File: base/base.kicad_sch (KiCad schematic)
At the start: 6 parts, among them J1 DF40GB(1.5)-30DS-0.4V(51), J2 DIP-48_Socket

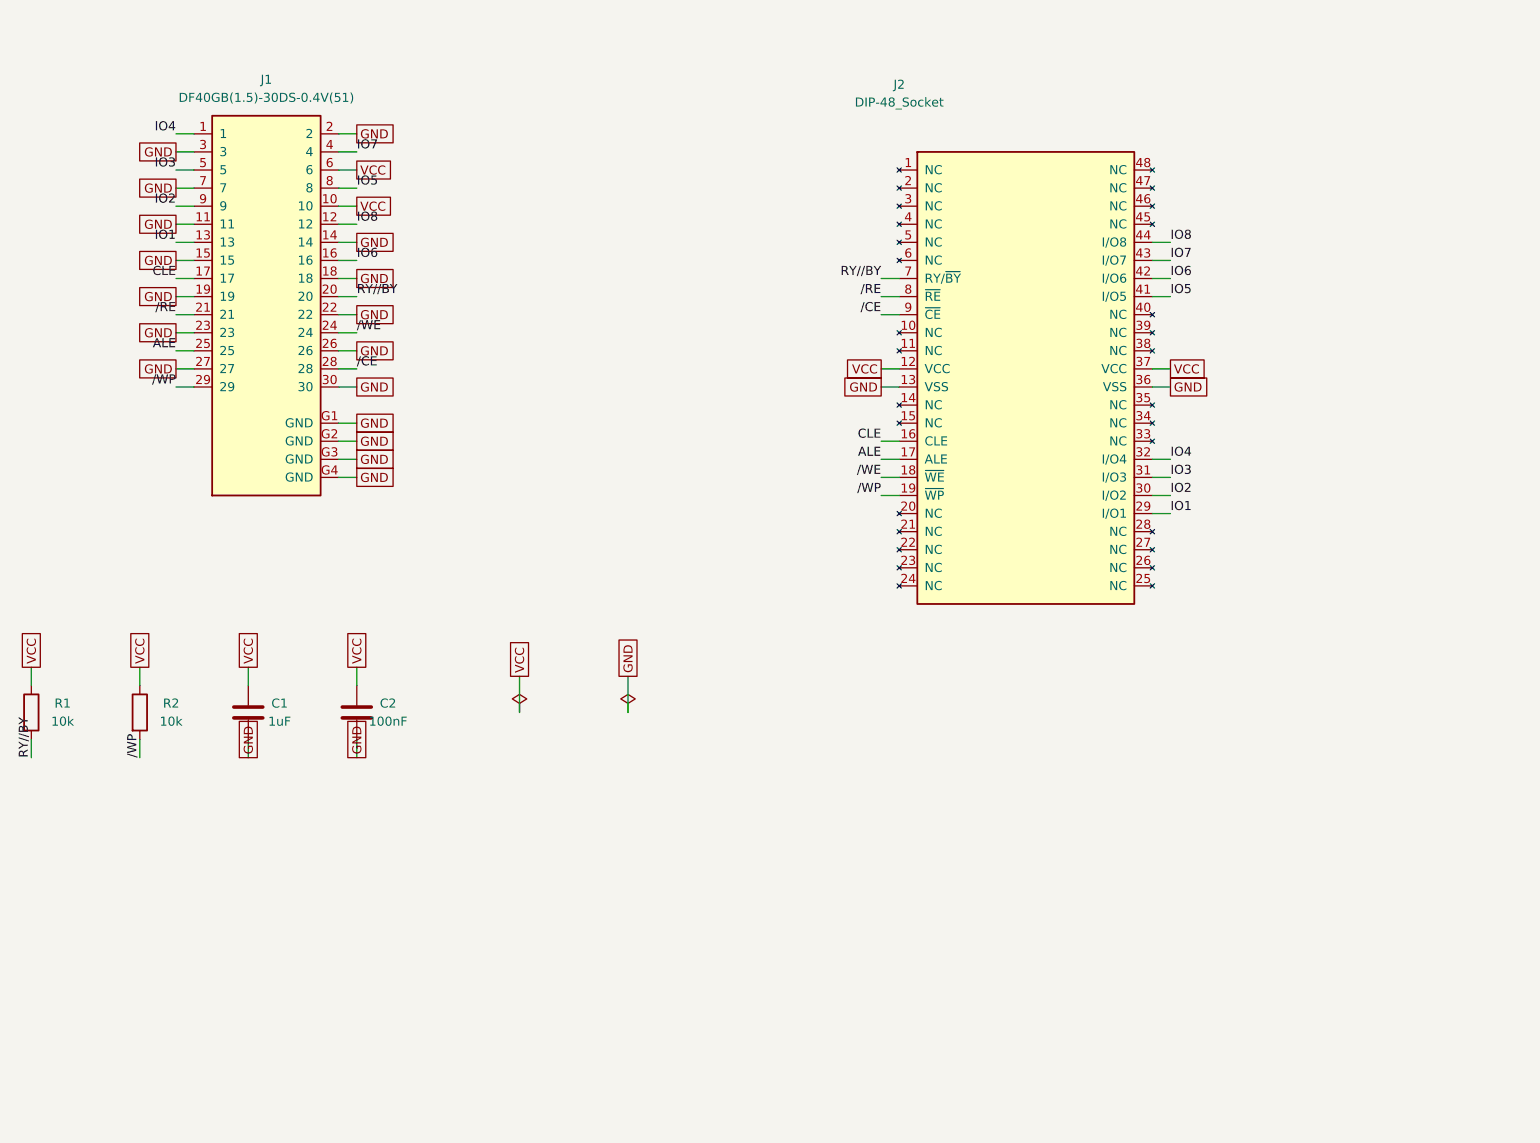
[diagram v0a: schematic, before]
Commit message: Regenerate the panel against Alex's second silk pass
Carrier silk warnings 20 -> 6: the four pin-number texts are gone and U1's
B.SilkS no longer runs off the board edge. What is left is REV A and
VFBGA67, still 0.85 mm / 0.106 mm against JLC's 1.0 / 0.15 legend minimum,
and both crossing J1's silk rectangle.

Panel: 56.80 x 49.60 mm, 16 up, 412 mouse bites, no hard violations.

Also fixed two cosmetic bugs in panelize.sh's own summary -- the board-count
match was missing the library nickname prefix so it always printed 0, and
the outline-extent regex required (layer "Edge.Cuts") at a fixed offset from
(start ...), which it is not, so the size line never printed. Neither
affected the panel itself.
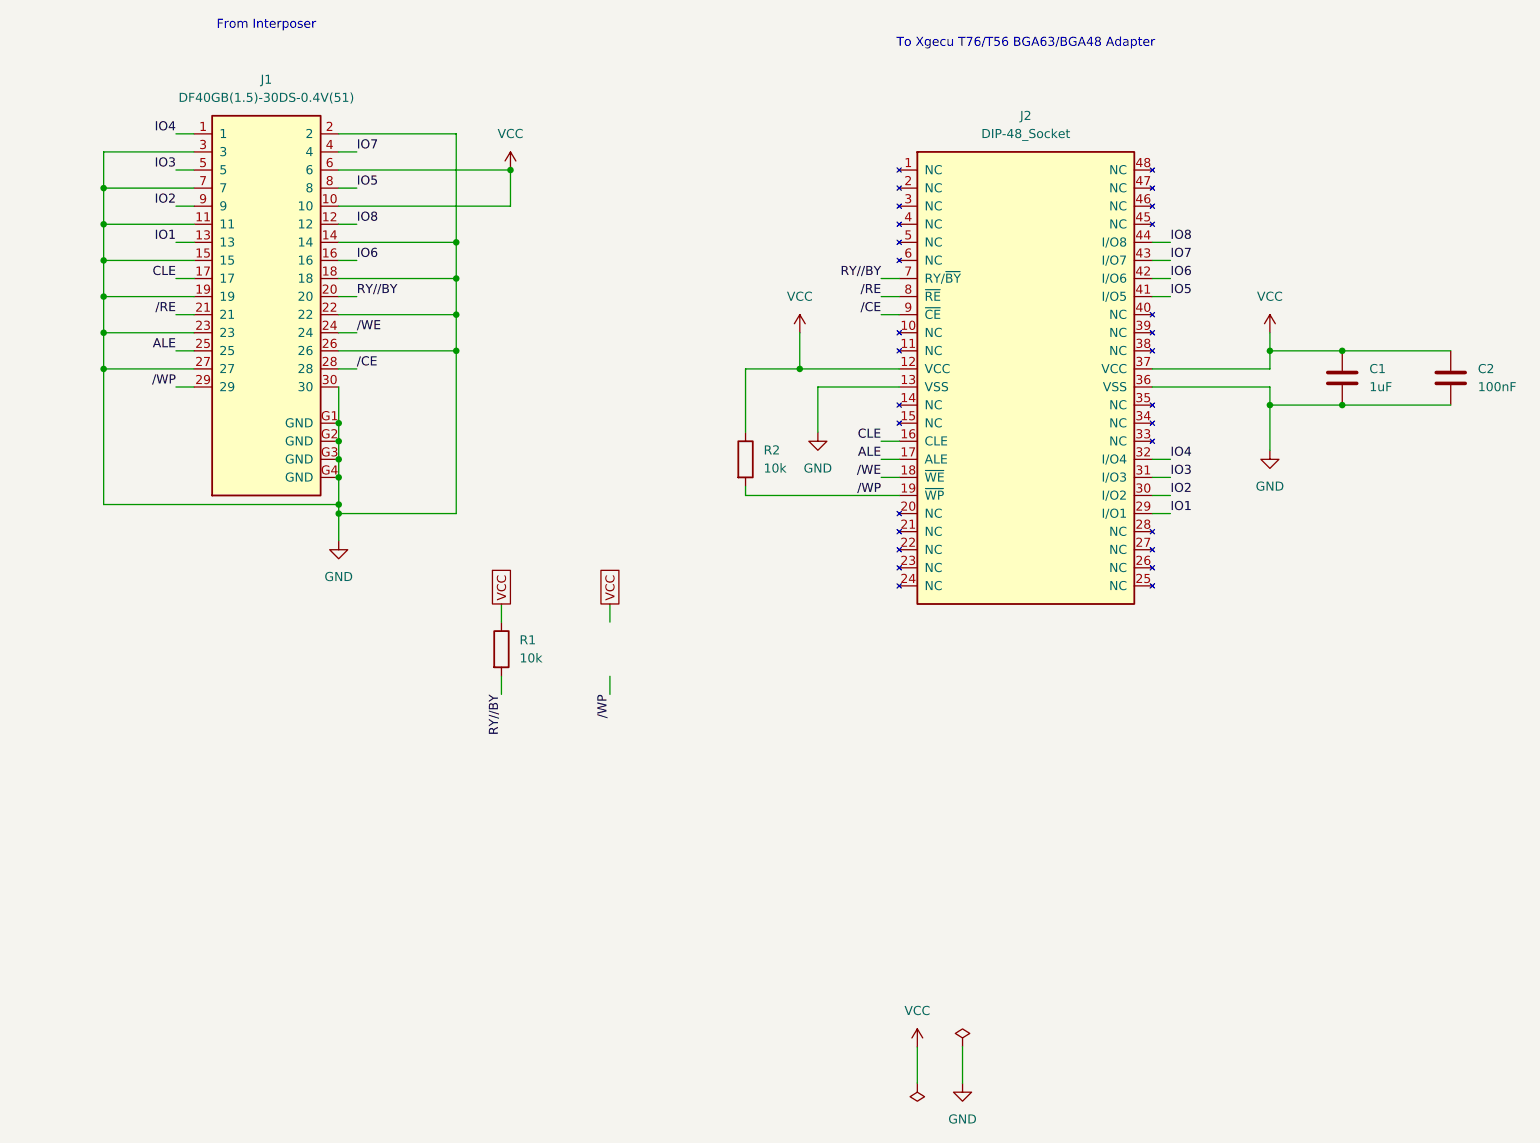
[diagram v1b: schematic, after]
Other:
- note added: "From Interposer"
- note added: "To Xgecu T76/T56 BGA63/BGA48 Adapter"
- moved on the sheet: C1, C2, R1, R2

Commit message: Finish base routing: 16 of 17 connections
tools/route_base.py is additive and re-runnable. It removes only its own
output -- vias and inner-layer tracks -- so Alex's F.Cu/B.Cu hand routing
survives a rerun, and it plans the whole board before committing anything so
a bad net ordering can be thrown away rather than hand-unpicked.

Routed: IO1-IO4, /RE, /ALE, /WP, /WE, /CE, VCC J1.10 and J2.12<->J2.37, and
R1's pull-up tail. Six of these sit on the wrong side of J1 -- IO1-IO4 are on
the odd row but land on the right-hand DIP column, /WE and /CE the reverse --
so they drop to In1/In2 and cross under the connector.

The zone was the reason every J1 GND pad read unconnected: it was on KiCad's
stock 0.5 mm clearance / 0.25 min width / 0.5 thermal gap, and a pour on those
settings cannot approach a 0.4 mm-pitch connector from any direction. Now on
the carrier's 0.2 / 0.15 / 0.3 with solid pad connection. 0.15 is load-bearing:
at 0.25 the pour needs 0.65 mm to reach a GND pad between two escape stubs and
has exactly 0.65, and all 13 go unconnected again.

Bugs found and fixed in my own checker along the way, each caught by DRC
rather than by reading the code:
  - pads were obstacles on every layer, so J1's B.Cu pads walled off both
    inner layers under the connector -- exactly the space the crossing nets
    need
  - track width was assumed 0.15, but Power-class runs are 0.4, under-
    reporting clearance to the VCC tracks by 0.125 mm
  - hole-to-hole was skipped for same-net pads and same-net vias, which
    stacked stitching vias on escape vias (18 holes_co_located)
  - the board edge was taken as a bounding box, but base's outline carries
    (radius 3), so stitching vias landed in corners that do not exist
  - strip() dropped its references to removed items, and pcbnew then freed
    them under the board; GetArea() started returning raw SwigPyObjects

DRC: no clearance, hole or edge violations, 0 unrouted signal nets.

Still open, both needing a decision rather than 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
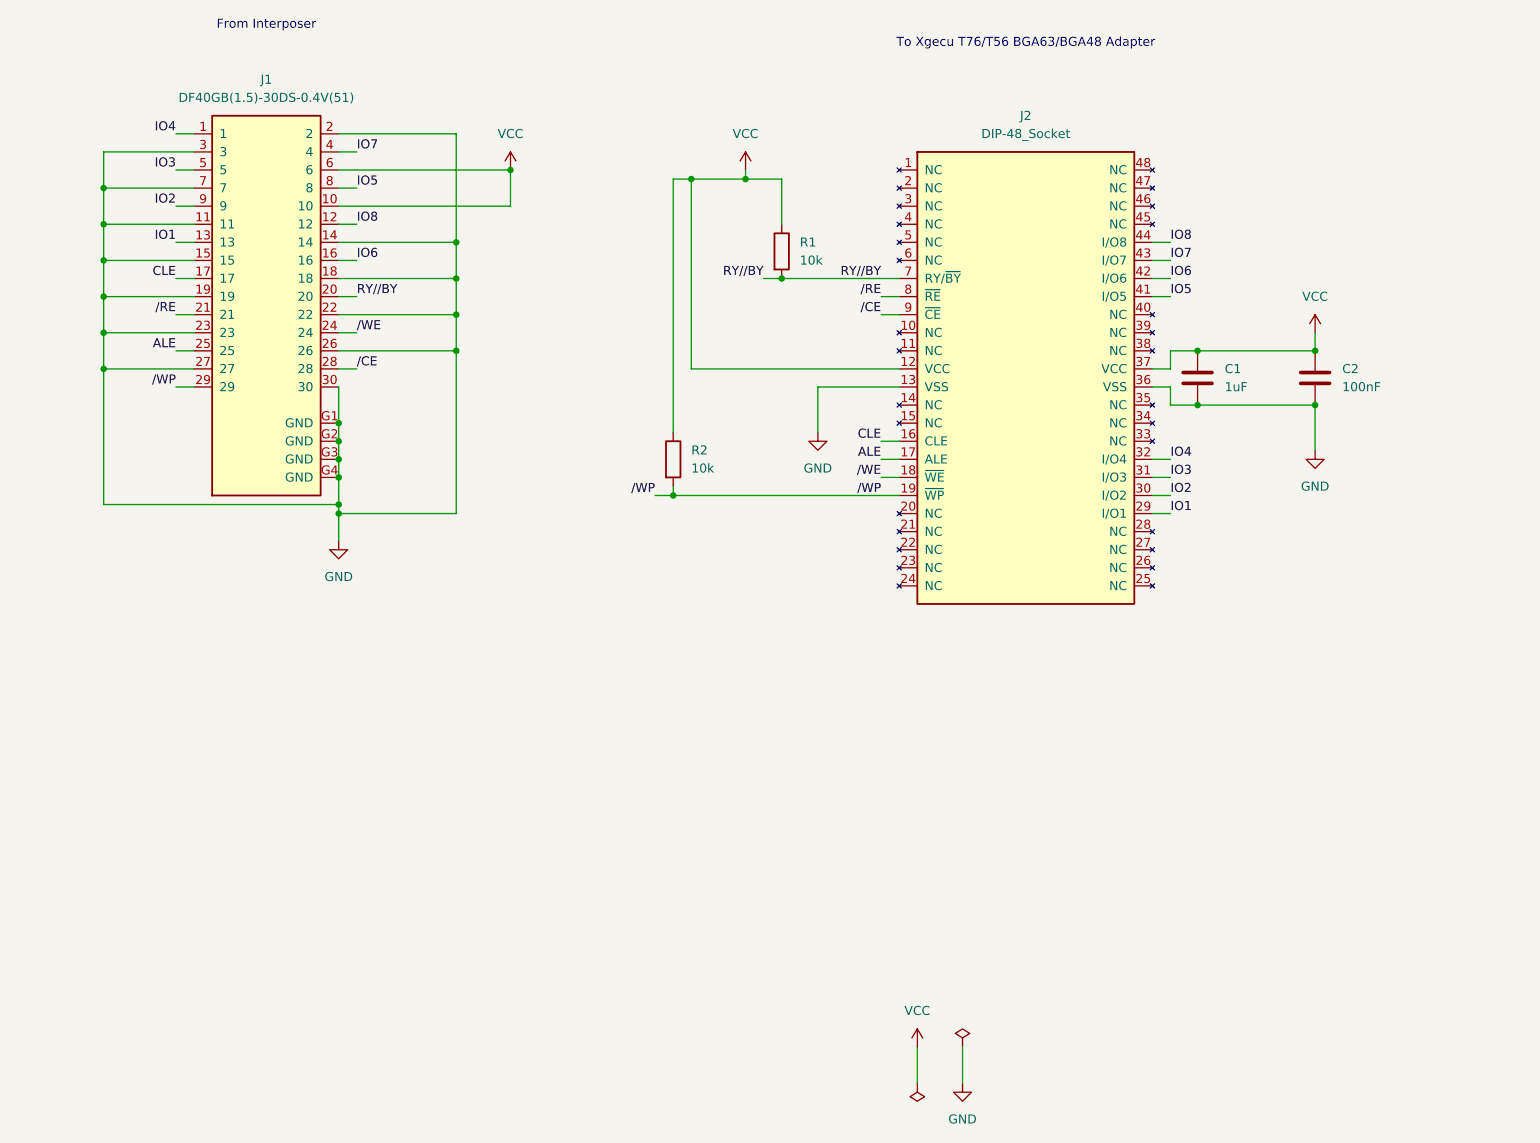
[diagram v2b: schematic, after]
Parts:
- C1: footprint Capacitor_SMD:C_0603_1608Metric -> Capacitor_SMD:C_0603_1608Metric_Pad1.08x0.95mm_HandSolder
- C2: footprint Capacitor_SMD:C_0402_1005Metric -> Capacitor_SMD:C_0603_1608Metric_Pad1.08x0.95mm_HandSolder
- R1, R2: footprint Resistor_SMD:R_0402_1005Metric -> Resistor_SMD:R_0603_1608Metric_Pad0.98x0.95mm_HandSolder
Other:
- moved on the sheet: C1, C2, R1, R2
